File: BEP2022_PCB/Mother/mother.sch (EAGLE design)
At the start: 10 parts, among them U1 MCP2562-E/P, X1 JST-XH-03-PIN-LONG-PAD, X2 JST-XH-04-PIN-LONG-PAD, X3 JST-XH-04-PIN-LONG-PAD, X4 JST-XH-03-PIN-LONG-PAD

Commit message: update PCB
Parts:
- removed U$2: BAT, BAT:BAT
- added C1, C2, C3, C4: 4.7uF, SparkFun-Capacitors:4.7UF-0603-6.3V-(10%)
- added JP1: (no value), pinhead:PINHD-1X10
- added R2, R3: 1k, SparkFun-Resistors:1KOHM-0603-1/10W-1%
- added R4: 4.7k, SparkFun-Resistors:4.7KOHM-0603-1/10W-1%
- added U$3: (no value), AE-BNO055:AE-BNO055-BO
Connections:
- removed net AIN_5V: J1.7, X4-1.S
- new net CS: JP1.2, U$1.IO4
- new net DI: JP1.3, U$1.IO23
- new net DO: JP1.7, U$1.IO19
- new net EN: C1.2, U$1.EN
- new net N$1: JP1.1
- new net N$10: JP1.10
- new net N$8: JP1.8
- new net N$9: JP1.9
- new net SCL: R2.1, U$1.IO22, U$3.SCL
- new net SCLK: JP1.5, U$1.IO18
- new net SDA: R3.1, U$1.IO21, U$3.SDA
- net 1WIRE: now also R4.1
- net 3V3: now also C2.1, C3.1, C4.1, JP1.4, R2.2, R3.2, R4.2, U$3.VIN, X4-2.S
- net AIN: now also U$1.IO32, X4-1.S; no longer J2.4, U$1.IO27
- net GND: now also C1.1, C2.2, C3.2, C4.2, JP1.6, U$3.GND; no longer U$2.-
- net VDD_5V: no longer U$2.+, X4-2.S

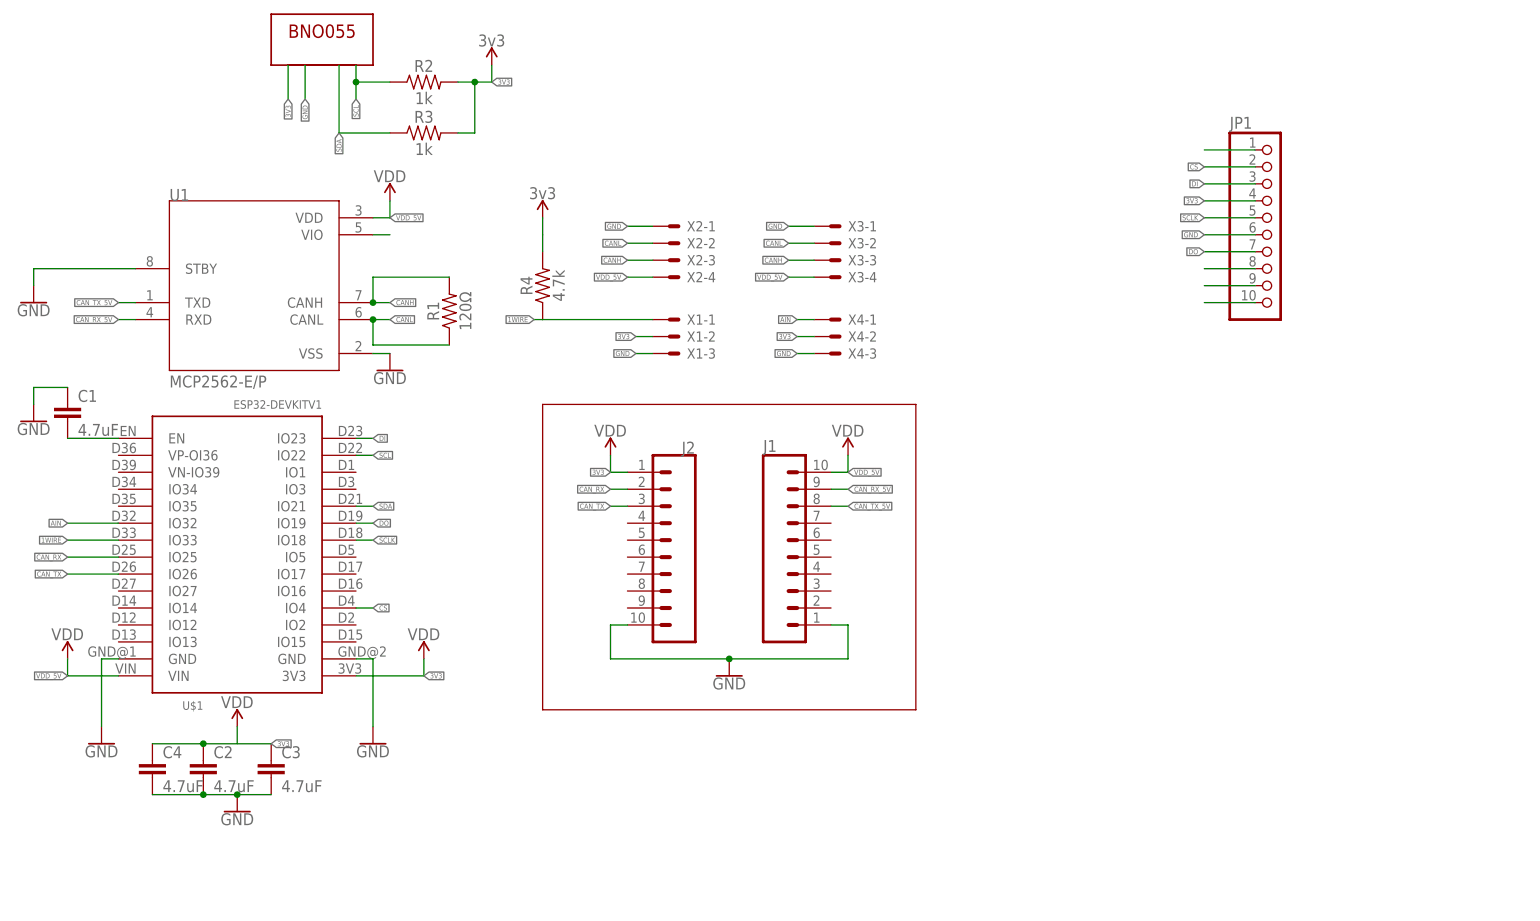
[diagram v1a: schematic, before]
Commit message: 母機の基板設計をした
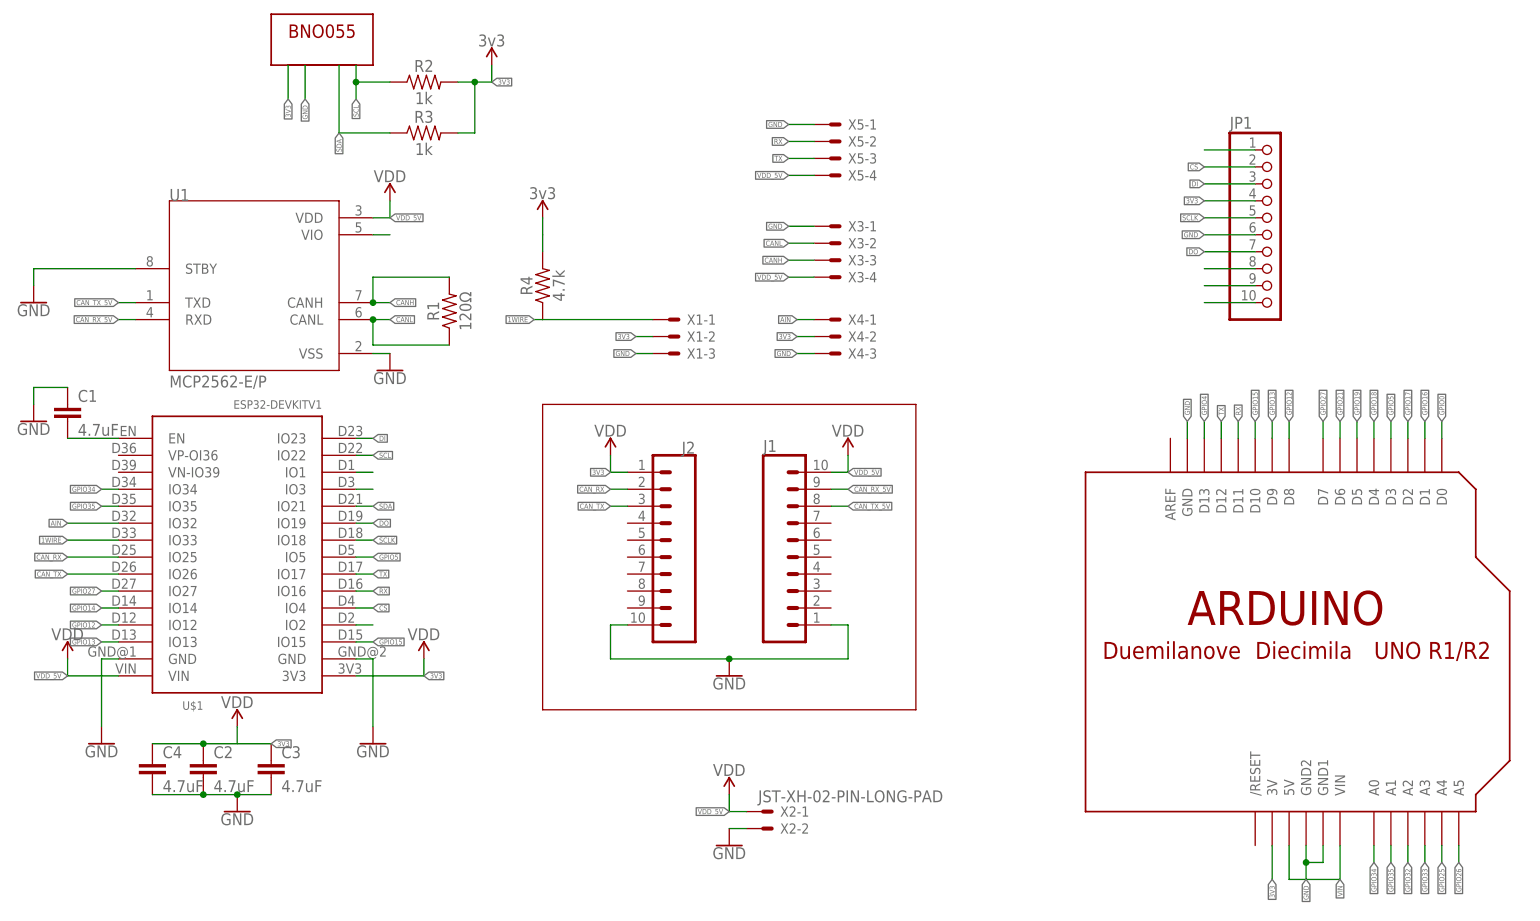
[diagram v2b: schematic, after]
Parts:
- added U$2: ARDUINO-NOHOLE, adafruit:ARDUINO-NOHOLE
- added X5: JST-XH-04-PIN-LONG-PAD, JST XH Connectors:JST-XH-04-PIN-LONG-PAD
- X2: value JST-XH-04-PIN-LONG-PAD -> JST-XH-02-PIN-LONG-PAD; device JST XH Connectors:JST-XH-04-PIN-LONG-PAD -> JST XH Connectors:JST-XH-02-PIN-LONG-PAD
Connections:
- new net GPIO0: U$2.D0
- new net GPIO1: U$1.IO1
- new net GPIO12: U$1.IO12, U$2.D8
- new net GPIO13: U$1.IO13, U$2.D9
- new net GPIO14: U$1.IO14
- new net GPIO15: U$1.IO15, U$2.D10
- new net GPIO16: U$2.D1
- new net GPIO17: U$2.D2
- new net GPIO18: U$2.D4
- new net GPIO19: U$2.D5
- new net GPIO21: U$2.D6
- new net GPIO25: U$2.A4
- new net GPIO26: U$2.A5
- new net GPIO27: U$1.IO27, U$2.D7
- new net GPIO32: U$2.A2
- new net GPIO33: U$2.A3
- new net GPIO34: U$1.IO34, U$2.A0
- new net GPIO35: U$1.IO35, U$2.A1
- new net GPIO4: U$2.D13
- new net GPIO5: U$1.IO5, U$2.D3
- new net N$2: U$1.IO3
- new net N$5: U$1.IO2
- new net RX: U$1.IO16, U$2.D11, X5-2.S
- new net TX: U$1.IO17, U$2.D12, X5-3.S
- new net VIN: U$2.5V, U$2.VIN
- net 3V3: now also U$2.3V
- net CANH: no longer X2-3.S
- net CANL: no longer X2-2.S
- net GND: now also U$2.GND, U$2.GND1, U$2.GND2, X2-2.S, X5-1.S; no longer X2-1.S
- net VDD_5V: now also X2-1.S, X5-4.S; no longer X2-4.S
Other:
- moved on the sheet: X2-1, X2-2
